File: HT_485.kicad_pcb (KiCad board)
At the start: 2 copper layers, 75 x 40 mm, 45 parts, among them J1 POWER, J2 485, SW1 EDS05SGRSTR04Q, U1 ISL3179EIBZ, U2 SHT31-DIS-P2.5KS, U3 LM2576D2TR4-3.3G, U4 STM32L010F4P6

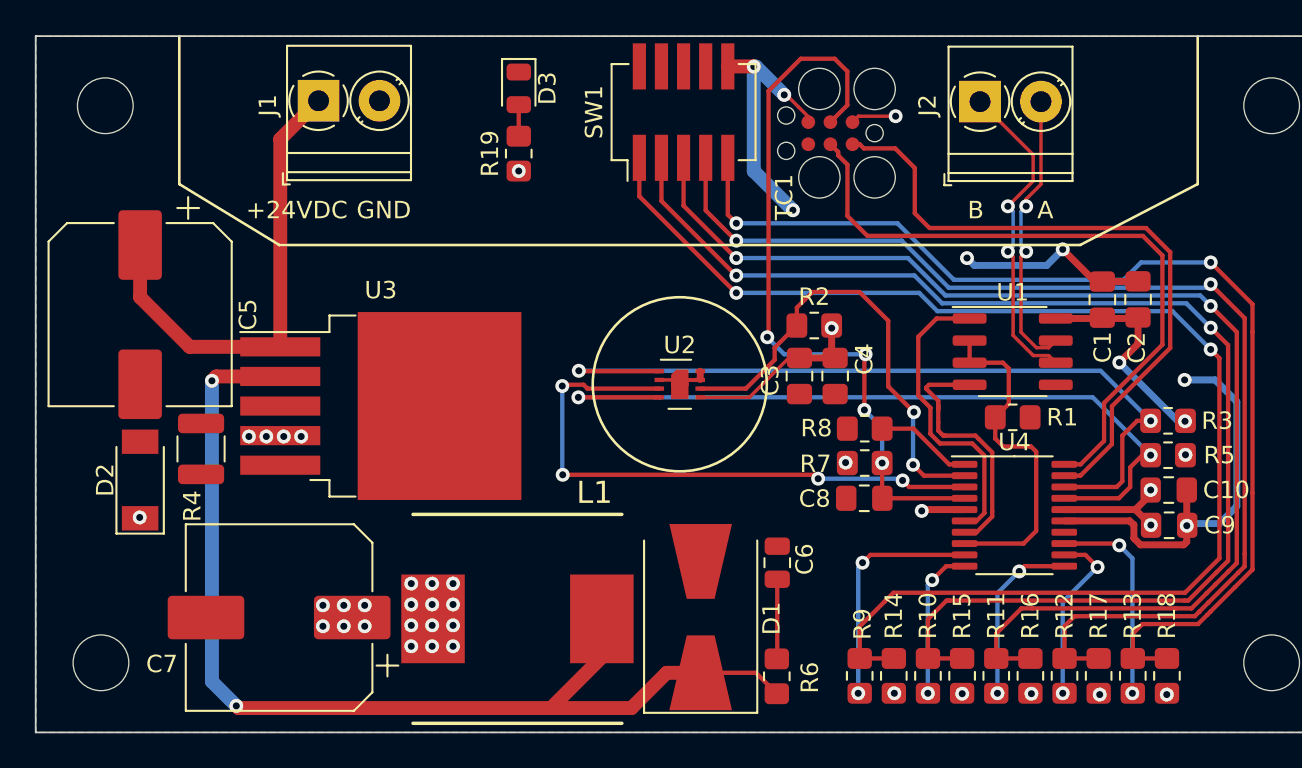
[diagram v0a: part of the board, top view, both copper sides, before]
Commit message: Adattato master a scatola
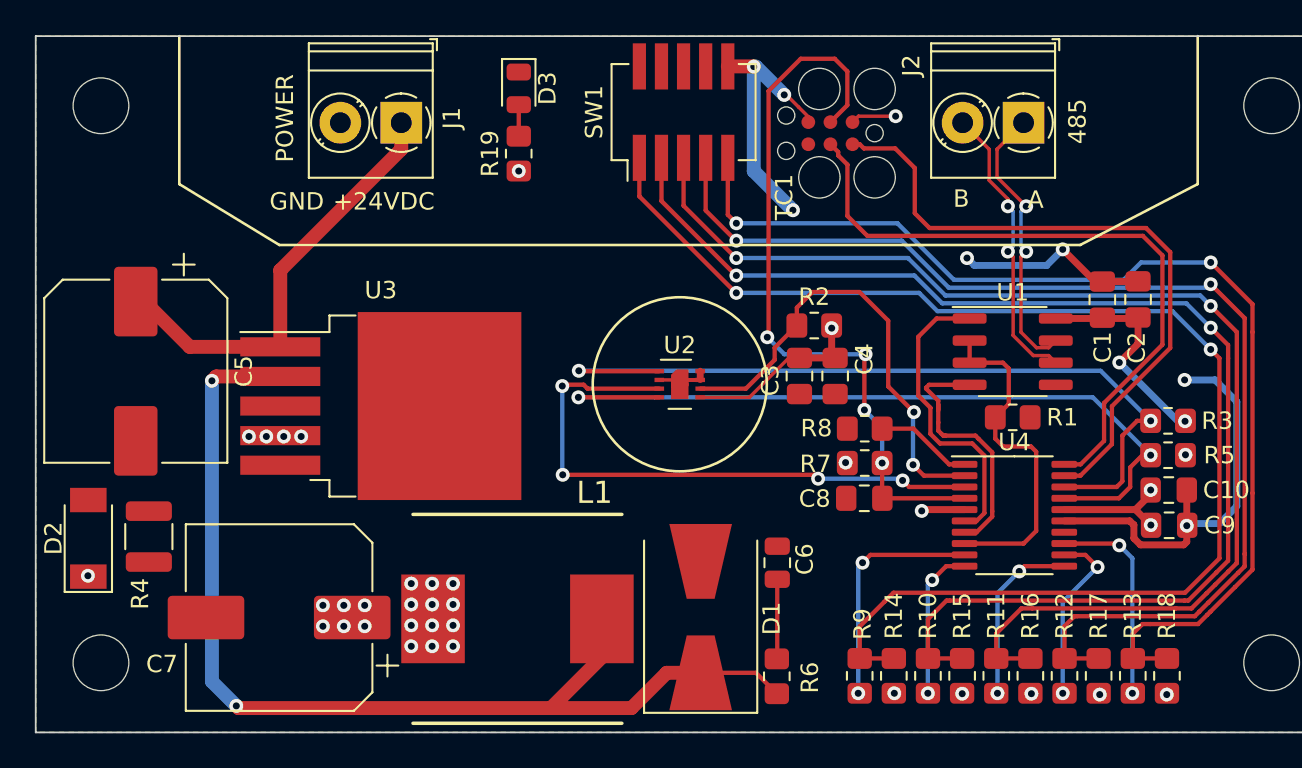
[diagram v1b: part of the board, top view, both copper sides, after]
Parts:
- moved R4 5.86 mm to (116.5, 94.8)
- moved J1 4.91 mm to (131.0, 71.0), turned to 180 degrees
- moved D2 4.48 mm to (113.0, 94.8)
- moved C5 3.26 mm to (115.8, 85.2)
- moved J2 2.78 mm to (166.8, 71.0), turned to 180 degrees
- moved REF** 0.25 mm to (113.8, 70.0)
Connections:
- J2 pad 1: /485- -> /485+
- J2 pad 2: /485+ -> /485-
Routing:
- net +24V: track 27.3 -> 25.0 mm
- net /485-: track 18.8 -> 16.8 mm

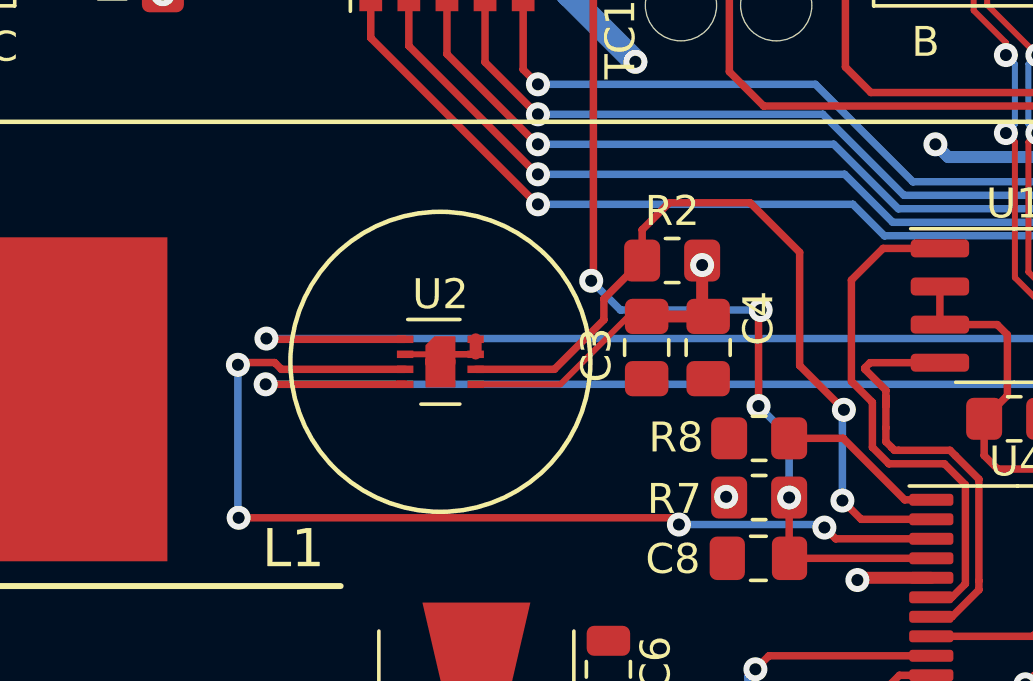
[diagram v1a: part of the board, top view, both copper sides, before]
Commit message: Modificata posizione resistenze
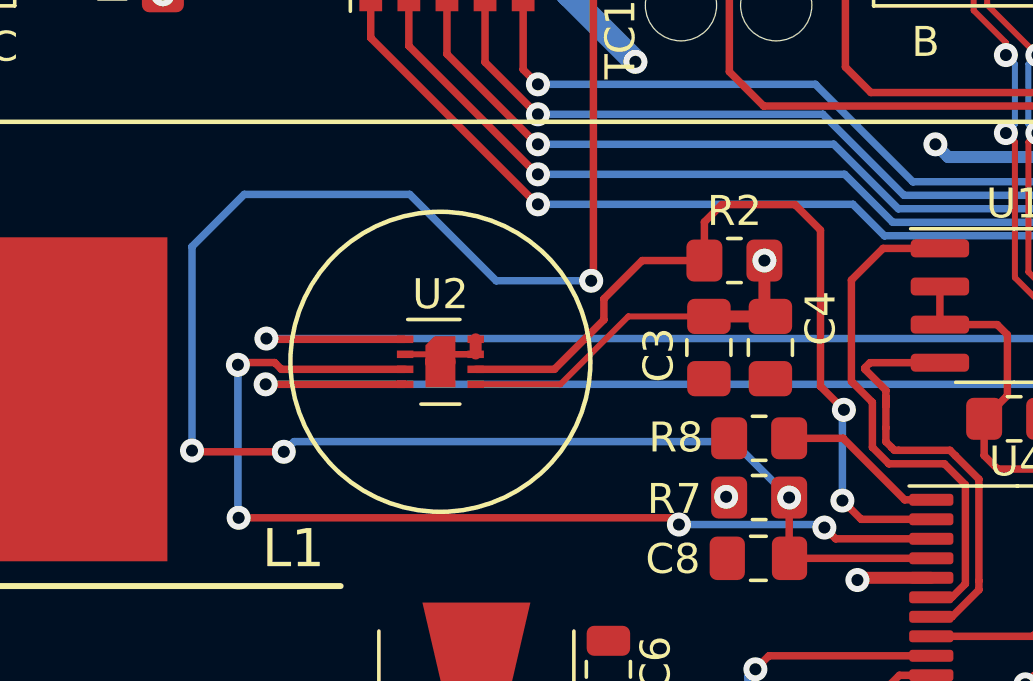
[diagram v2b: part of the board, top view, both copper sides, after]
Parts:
- moved R2 2.08 mm to (156.8, 82.6)
- moved C3 2.07 mm to (155.9, 85.5)
- moved C4 2.07 mm to (158.0, 85.5)
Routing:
- net /NRESET: track 42.6 -> 72.7 mm
- net +3V3: track 35.5 -> 37.7 mm
- net /RESET: track 26.9 -> 27.9 mm

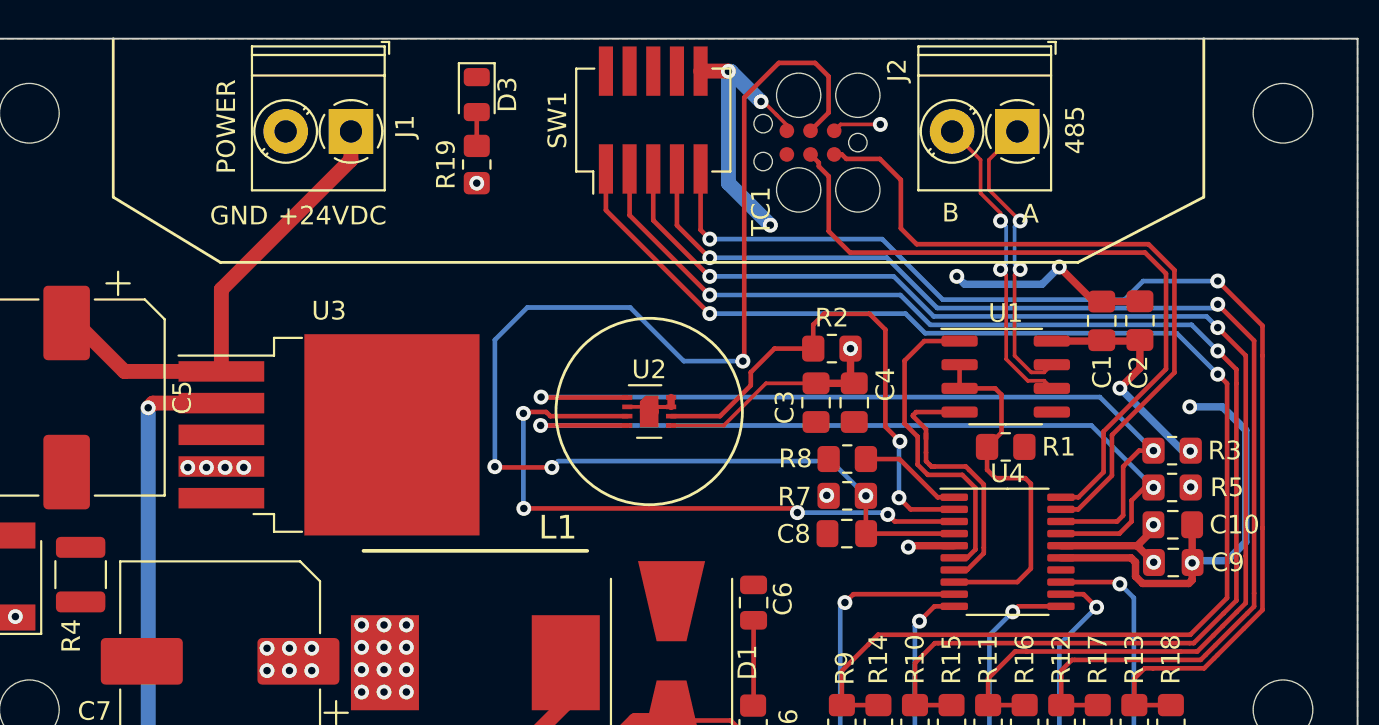
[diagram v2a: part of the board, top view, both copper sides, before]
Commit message: Aggiunto terminatore 485
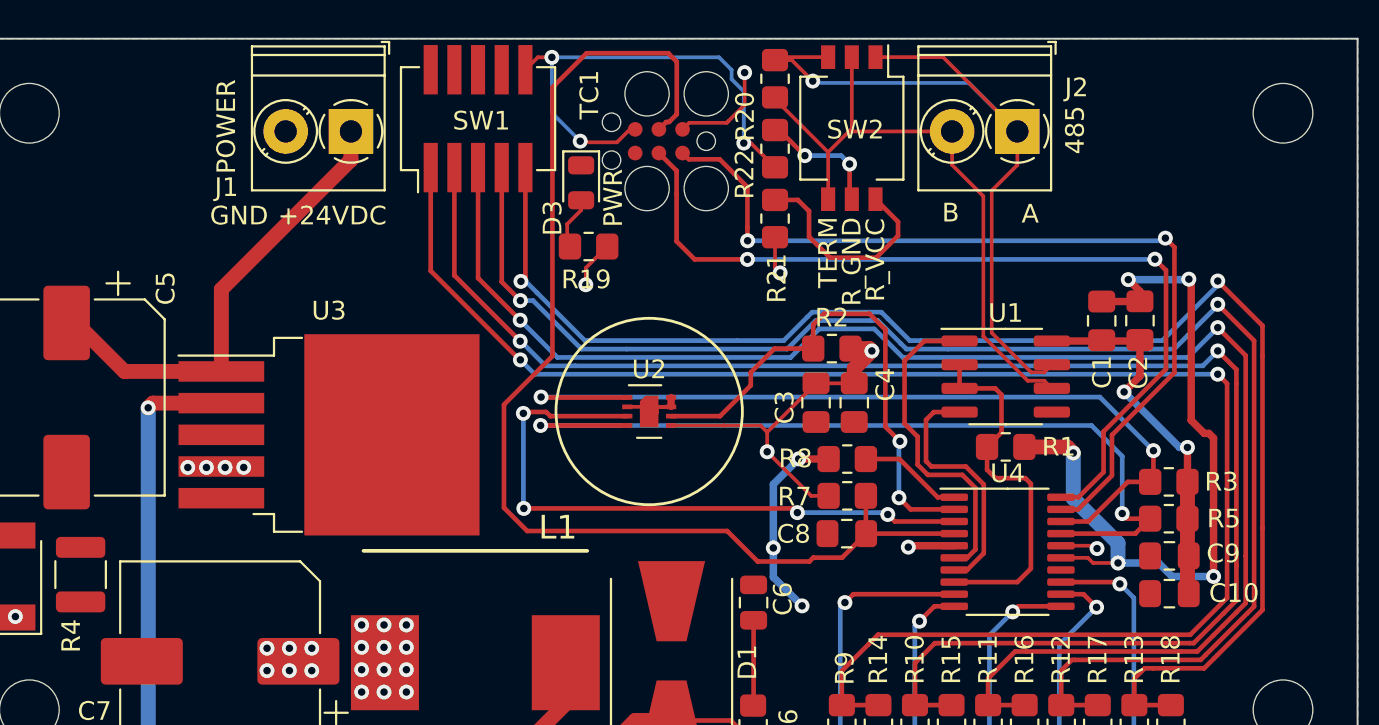
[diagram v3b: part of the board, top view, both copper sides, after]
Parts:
- added R20: 120R, Resistor_SMD:R_0805_2012Metric_Pad1.20x1.40mm_HandSolder, F.Cu at (153.8, 68.2)
- added R21: 370R, Resistor_SMD:R_0805_2012Metric_Pad1.20x1.40mm_HandSolder, F.Cu at (153.8, 75.7)
- added R22: 370R, Resistor_SMD:R_0805_2012Metric_Pad1.20x1.40mm_HandSolder, F.Cu at (153.8, 71.9)
- added SW2: 416131160803, Button_Switch_SMD:SW_DIP_SPSTx03_Slide_KingTek_DSHP03TS_W7.62mm_P1.27mm, F.Cu at (157.9, 70.8)
- moved SW1 9.40 mm to (137.8, 70.3)
- moved TC1 8.13 mm to (147.5, 71.5)
- moved R19 7.44 mm to (143.8, 77.2), turned to 180 degrees
- moved D3 7.33 mm to (143.3, 73.7)
- moved C10 3.70 mm to (174.9, 95.8), turned to 0 degrees
- moved R3 1.68 mm to (174.9, 89.8)
- moved R5 1.68 mm to (174.9, 91.8)
- moved C9 0.41 mm to (174.9, 93.7), turned to 0 degrees
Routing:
- net GND: track 54.6 -> 82.9 mm, vias 7 -> 11
- net /485+: track 16.3 -> 42.4 mm, vias 2 -> 1
- net /485-: track 16.8 -> 34.3 mm, vias 2 -> 0
- net +3V3: track 37.7 -> 54.8 mm, vias 38 -> 37
- net Net-(R13-Pad1): track 63.4 -> 78.1 mm
- net Net-(R12-Pad1): track 66.6 -> 80.9 mm
- net Net-(R11-Pad1): track 69.7 -> 83.6 mm
- net Net-(R10-Pad1): track 73.7 -> 85.7 mm
- net Net-(SW2-Pad6): track 0.00 -> 11.6 mm
- net Net-(R14-Pad2): track 77.0 -> 88.3 mm
- net /NRESET: track 72.7 -> 63.4 mm, vias 4 -> 0
- net /SWDIO: track 38.2 -> 47.4 mm, vias 0 -> 2
- net /SWCLK: track 38.4 -> 47.1 mm, vias 0 -> 2
- net Net-(SW2-Pad5): track 0.00 -> 6.69 mm, vias 0 -> 2
- net /TX: track 14.9 -> 13.5 mm
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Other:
- board text added: "R_GND"
- board text added: "R_VCC"
- board text added: "TERM"

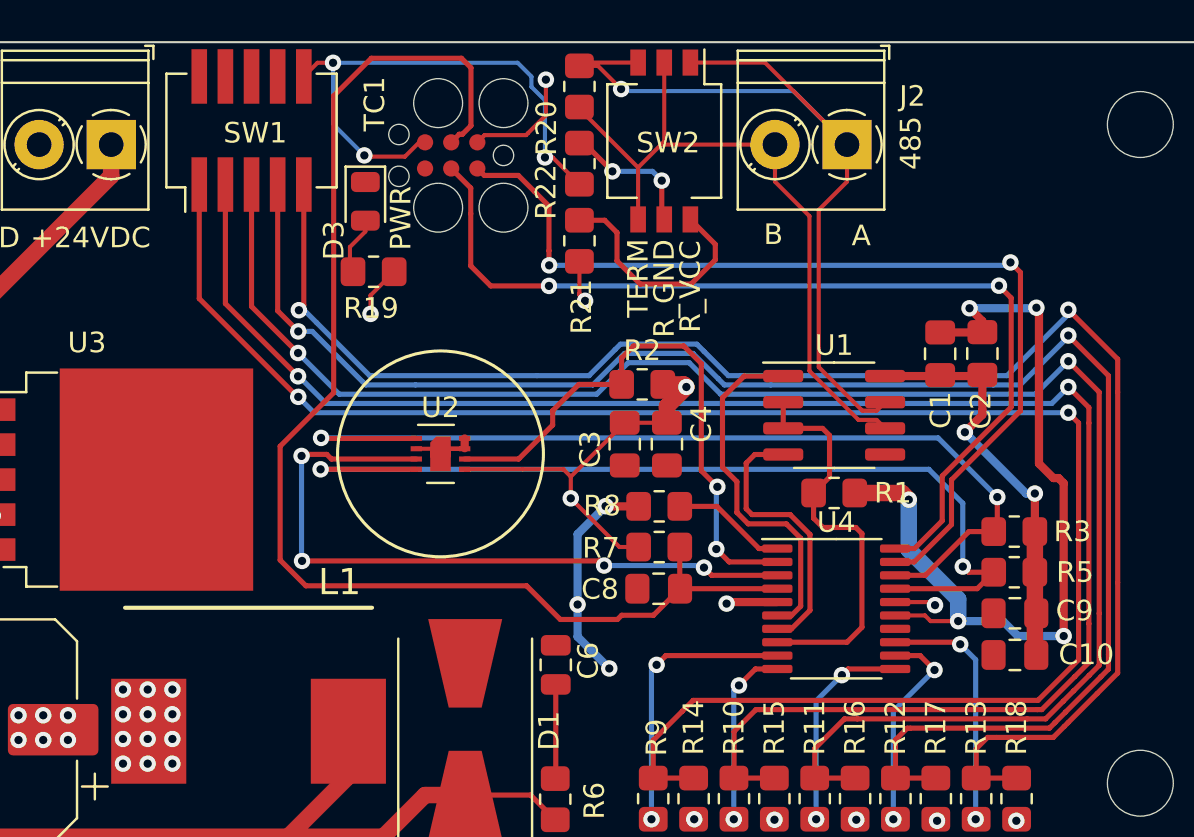
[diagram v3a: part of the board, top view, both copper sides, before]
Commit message: Rivisti dip switch con solder jumper
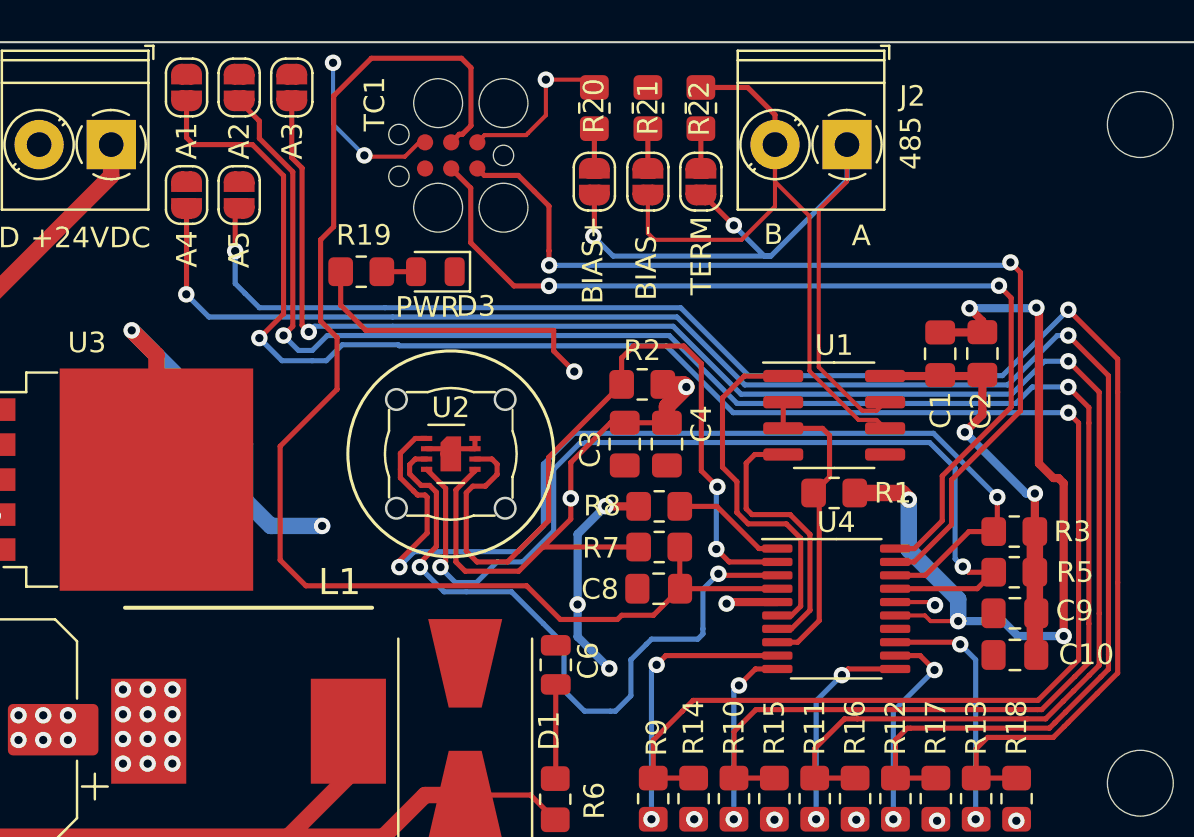
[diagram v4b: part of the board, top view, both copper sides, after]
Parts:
- removed SW1: EDS05SGRSTR04Q, Button_Switch_SMD:SW_DIP_SPSTx05_Slide_KingTek_DSHP05TJ_W5.25mm_P1.27mm_JPin
- removed SW2: 416131160803, Button_Switch_SMD:SW_DIP_SPSTx03_Slide_KingTek_DSHP03TS_W7.62mm_P1.27mm
- added JP1: BIAS+, Jumper:SolderJumper-2_P1.3mm_Open_RoundedPad1.0x1.5mm, F.Cu at (154.5, 72.8)
- added JP2: BIAS-, Jumper:SolderJumper-2_P1.3mm_Open_RoundedPad1.0x1.5mm, F.Cu at (157.1, 72.8)
- added JP3: TERMINATOR, Jumper:SolderJumper-2_P1.3mm_Open_RoundedPad1.0x1.5mm, F.Cu at (159.7, 72.8)
- added JP4: A1, Jumper:SolderJumper-2_P1.3mm_Open_RoundedPad1.0x1.5mm, F.Cu at (134.7, 68.2)
- added JP5: A3, Jumper:SolderJumper-2_P1.3mm_Open_RoundedPad1.0x1.5mm, F.Cu at (139.8, 68.2)
- added JP6: A5, Jumper:SolderJumper-2_P1.3mm_Open_RoundedPad1.0x1.5mm, F.Cu at (137.2, 73.4)
- added JP7: A2, Jumper:SolderJumper-2_P1.3mm_Open_RoundedPad1.0x1.5mm, F.Cu at (137.2, 68.2)
- added JP8: A4, Jumper:SolderJumper-2_P1.3mm_Open_RoundedPad1.0x1.5mm, F.Cu at (134.7, 73.4)
- added SF2: SF2, HT485:SF2, F.Cu at (147.5, 86.0)
- R20: value 120R -> 370R
- R22: value 370R -> 120R
- U2: value SHT31-DIS-P2.5KS -> SHT31-DIS + SF2; footprint Sensor_Humidity:Sensirion_DFN-8-1EP_2.5x2.5mm_P0.5mm_EP1.1x1.7mm -> HT485:Sensirion_DFN-8-1EP_2.5x2.5mm_P0.5mm_EP1.1x1.7mm
- moved R21 7.26 mm to (157.1, 69.2)
- moved R22 6.49 mm to (159.7, 69.2), turned to 90 degrees
- moved D3 4.82 mm to (146.8, 77.2), turned to 180 degrees
- moved R20 1.28 mm to (154.5, 69.2)
- moved R19 0.60 mm to (143.2, 77.2), turned to 0 degrees
- moved U2 0.50 mm to (147.5, 86.0)
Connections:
- R20 pad 1: /485+ -> +3V3
- R20 pad 2: /485- -> Net-(JP1-Pad2)
- R21 pad 1: +3V3 -> Net-(JP2-Pad2)
- R21 pad 2: Net-(SW2-Pad6) -> GND
- R22 pad 2: GND -> /485-
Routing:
- net +3V3: track 54.8 -> 75.8 mm, vias 37 -> 36
- net Net-(SW2-Pad6): track 11.6 -> 0.00 mm
- net /RESET: track 27.9 -> 37.9 mm
- net Net-(JP4-Pad1): track 88.3 -> 95.4 mm
- net Net-(JP3-Pad1): track 6.69 -> 1.92 mm, vias 2 -> 0
- net /SDA: track 46.1 -> 50.6 mm
- net /485+: track 42.4 -> 38.3 mm, vias 1 -> 2
- net /DE: track 19.6 -> 15.6 mm
- net Net-(JP7-Pad1): track 85.7 -> 89.7 mm
- net GND: track 82.9 -> 86.3 mm, vias 11 -> 12
- net Net-(JP2-Pad2): track 0.00 -> 1.92 mm
- net Net-(JP1-Pad2): track 0.00 -> 1.92 mm
- net Net-(JP8-Pad1): track 80.9 -> 82.4 mm
- net Net-(JP5-Pad1): track 83.6 -> 84.9 mm
- net Net-(D3-Pad2): track 2.85 -> 1.66 mm
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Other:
- board text added: "BIAS+"
- board text added: "BIAS-"
- board text removed: "R_GND"
- board text removed: "R_VCC"
